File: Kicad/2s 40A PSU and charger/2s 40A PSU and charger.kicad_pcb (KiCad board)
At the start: 4 copper layers, 45 x 20 mm, 114 parts, among them J1 Keystone 3579, J10 G-Switch-GT-USB-7025, J11 1.27mm 4 pin socket, J12 USB, J2 JST XH-S Balance Plug, J3 Keystone 3579, J4 Keystone 3569, J5 Keystone 3569, J6 Keystone 3579, J7 Keystone 3579, J8 Keystone 3569, J9 Keystone 3569, Q1 PJA3430, Q2 PJA3430, Q3 Vishay sir404dp, or SiR500DP, Q4 PJA3430, Q5 PJA3430, Q6 Vishay sir404dp, or SiR500DP, U1 BQ76905RGRR, U2 AP63203WU, U3 BQ24780SRUYR, U5 THVD1420DRLR, U6 CH32X035G8U6, U7 TPS7A2633DRV

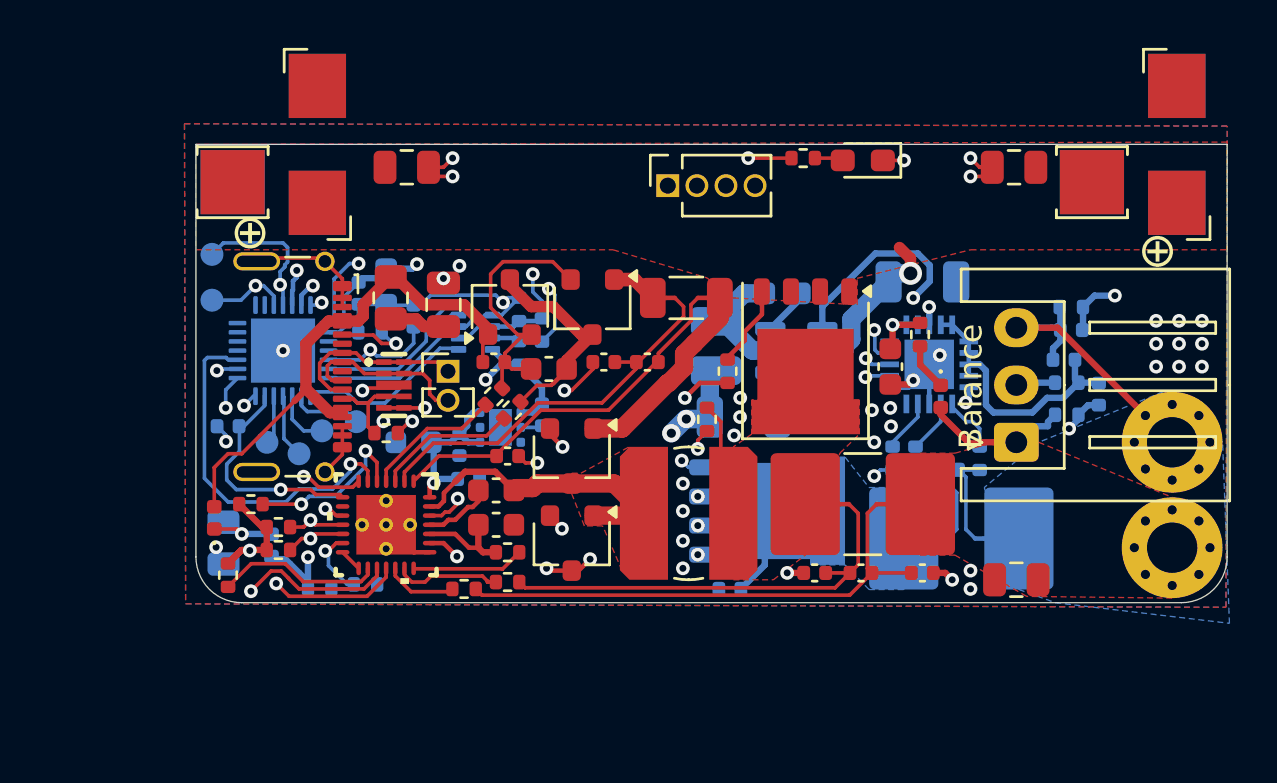
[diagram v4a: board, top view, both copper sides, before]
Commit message: Fixed incorrect mosfet pin assignments
This was an issue from the last test board I designed that I didn't catch. The mosfets have different pin assignments for drain, gate, and source, and I had messed those up in the schematic by choosing the wrong symbol. This should be fixed now
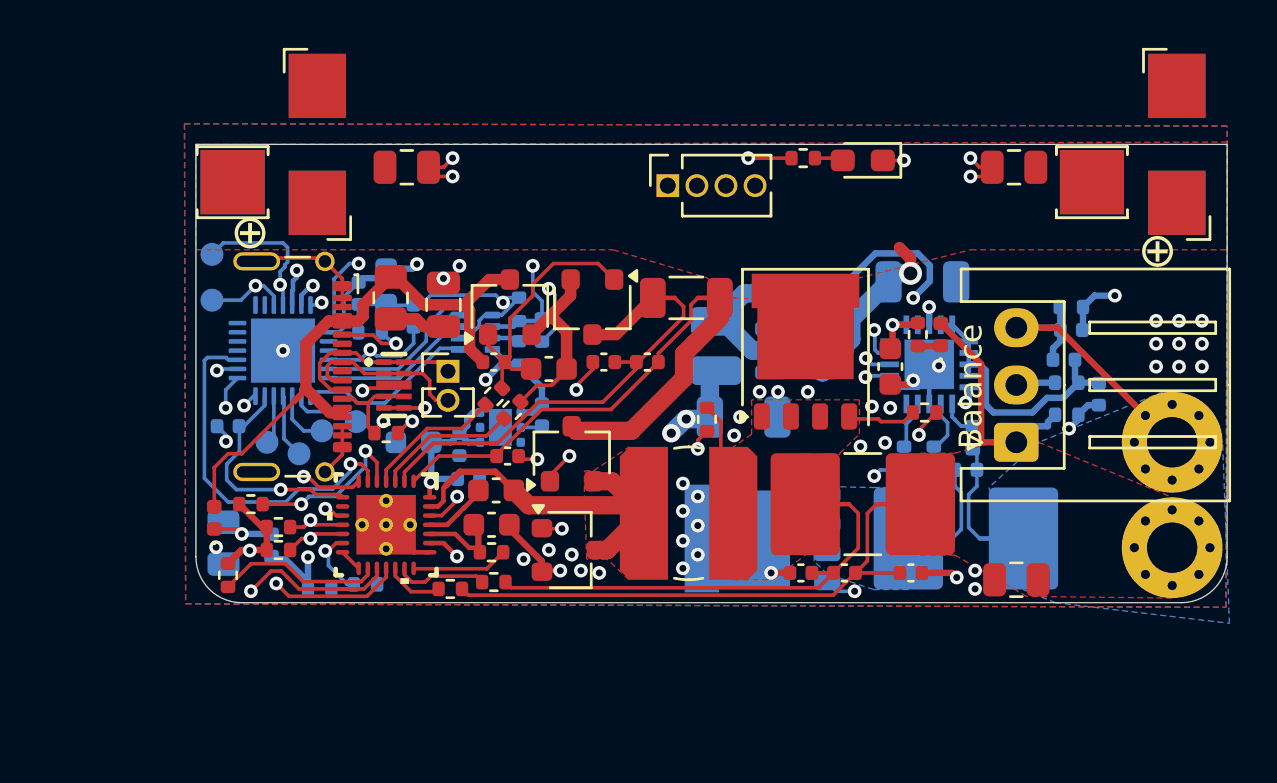
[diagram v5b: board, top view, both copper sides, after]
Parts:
- moved R10 8.79 mm to (139.9, 123.7), turned to 0 degrees
- moved C4 6.77 mm to (135.2, 125.8)
- moved D1 2.70 mm to (140.6, 120.3), turned to 90 degrees
- moved Q6 1.20 mm to (132.9, 129.2), turned to 180 degrees
- moved R4 0.95 mm to (142.0, 124.8)
- moved R5 0.80 mm to (140.3, 125.7)
- moved C3 0.80 mm to (141.7, 126.2)
- moved C22 0.72 mm to (136.4, 130.7)
- moved R20 0.70 mm to (121.0, 129.8)
- moved R21 0.60 mm to (121.1, 131.1)
- moved C21 0.60 mm to (134.5, 130.7)
- moved R22 0.60 mm to (119.2, 131.4)
- moved C23 0.50 mm to (139.3, 130.7)
- moved R6 0.50 mm to (139.0, 125.7)
- moved Q5 0.32 mm to (124.4, 129.7), turned to 0 degrees
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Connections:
- C4 pad 1: Net-(Q6-S) -> Net-(C4-Pad1)
- L2 pad 2: Net-(Q3-S) -> Net-(L2-Pad2)
- NT11 pad 1: Net-(Q6-S) -> Net-(C4-Pad1)
- NT6 pad 2: Net-(Q3-S) -> Net-(L2-Pad2)
- Q1 pad 1: /Battery Charger/IN -> Net-(Q1-G)
- Q1 pad 2: Net-(Q1-G) -> Net-(Q1-S)
- Q1 pad 3: Net-(Q1-S) -> /Battery Charger/IN
- Q2 pad 1: Net-(Q2-D) -> Net-(Q1-G)
- Q2 pad 2: Net-(Q1-G) -> Net-(Q1-S)
- Q2 pad 3: Net-(Q1-S) -> Net-(Q2-D)
- Q3 pad 1: /Battery Charger/MOTORPWR -> Net-(L2-Pad2)
- Q3 pad 2: /Battery Charger/MOTORPWR -> Net-(L2-Pad2)
- Q3 pad 3: /Battery Charger/MOTORPWR -> Net-(L2-Pad2)
- Q3 pad 5: Net-(Q3-S) -> /Battery Charger/MOTORPWR
- Q4 pad 1: Net-(Q4-D) -> Net-(Q4-G)
- Q4 pad 2: Net-(Q4-G) -> Net-(Q4-S)
- Q4 pad 3: Net-(Q4-S) -> Net-(Q4-D)
- Q5 pad 1: Net-(Q4-S) -> Net-(Q5-G)
- Q5 pad 2: Net-(Q5-G) -> GND
- Q5 pad 3: GND -> Net-(Q4-S)
- Q6 pad 1: GND -> Net-(C4-Pad1)
- Q6 pad 2: GND -> Net-(C4-Pad1)
- Q6 pad 3: GND -> Net-(C4-Pad1)
- Q6 pad 5: Net-(Q6-S) -> GND
- R12 pad 1: Net-(Q3-S) -> Net-(L2-Pad2)
- R14 pad 1: Net-(Q6-S) -> Net-(C4-Pad1)
- R18 pad 2: Net-(Q3-S) -> Net-(L2-Pad2)
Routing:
- net Net-(U3-BATDRV): track 29.5 -> 39.5 mm
- net GND: track 48.1 -> 53.6 mm, vias 43 -> 49
- net Net-(Q3-S): track 5.09 -> 0.00 mm
- net Net-(L2-Pad2): track 0.00 -> 5.09 mm
- net Net-(Q6-S): track 3.83 -> 0.00 mm
- net Net-(D1-A): track 2.62 -> 5.92 mm
- net Net-(Q4-S): track 14.8 -> 18.0 mm
- net Net-(Q6-G): track 10.6 -> 8.15 mm
- net /Battery Charger/IN: track 15.9 -> 18.2 mm
- net Net-(C4-Pad1): track 0.00 -> 1.51 mm
- net Net-(Q4-D): track 6.26 -> 7.61 mm
- net Net-(Q2-D): track 2.02 -> 3.30 mm
- net /Battery Balancer/-BAT: track 33.3 -> 32.1 mm
- net Net-(D1-K): track 2.08 -> 1.01 mm
- net Net-(Q1-S): track 6.71 -> 5.72 mm
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- added copper zone on B.Cu, net Net-(C4-Pad1)
- added copper zone on F.Cu, net Net-(L2-Pad2)
- removed copper zone on F.Cu, net Net-(Q3-S)
- removed copper zone on B.Cu, net Net-(Q6-S)

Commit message: Final tweaks, capacitor placement and GND keepouts
I tried my best to isolate signal grounds from the power paths. I also added a bunch of ground keepouts to help isolate.
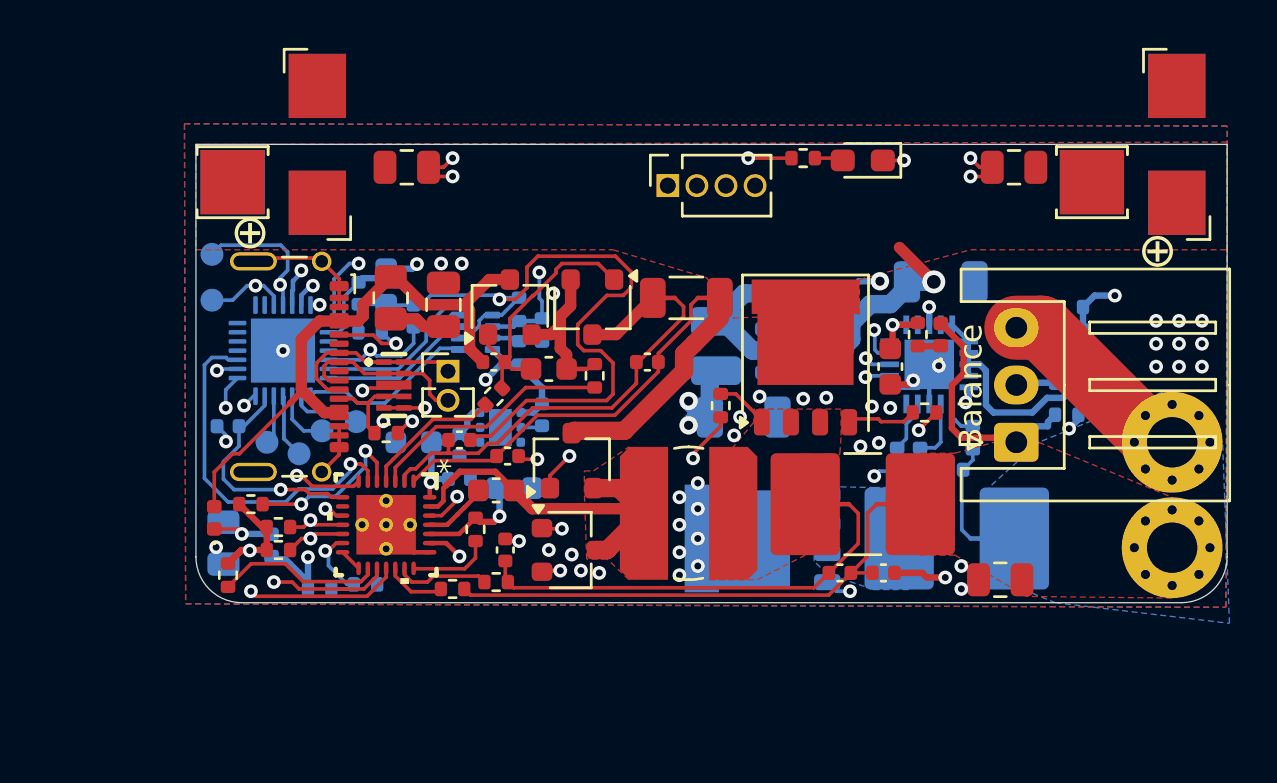
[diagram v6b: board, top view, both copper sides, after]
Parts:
- C24: moved to B.Cu
- moved C21 12.9 mm to (121.6, 129.7), turned to -90 degrees
- moved C9 7.16 mm to (119.6, 124.9), turned to 180 degrees
- moved R7 3.90 mm to (125.5, 122.1), turned to 90 degrees
- moved C24 1.89 mm to (122.0, 127.0)
- moved R20 1.22 mm to (120.3, 128.8), turned to 90 degrees
- moved NT14 1.21 mm to (124.9, 121.8), turned to 180 degrees
- moved C23 1.20 mm to (138.1, 130.7)
- moved R12 0.85 mm to (131.0, 123.4)
- moved C28 0.80 mm to (140.6, 118.0)
- moved C20 0.70 mm to (143.2, 131.0)
- moved R5 0.60 mm to (139.7, 125.8)
- moved C3 0.60 mm to (141.1, 126.2)
- moved C15 0.40 mm to (119.6, 126.6)
- moved NT1 0.40 mm to (142.1, 129.2)
- moved NT11 0.40 mm to (140.5, 129.2)
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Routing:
- net /Connectors/3.3v: track 63.6 -> 33.5 mm
- net GND: track 53.6 -> 72.1 mm, vias 49 -> 48
- net Net-(U3-CMSRC): track 6.14 -> 10.8 mm
- net /Battery Balancer/Balancer Alert: track 35.3 -> 37.8 mm
- net Net-(L2-Pad2): track 5.09 -> 3.13 mm
- net Net-(U3-BATSRC): track 30.2 -> 28.5 mm
- net /Battery Charger/MOTORPWR: track 8.54 -> 10.2 mm
- net Net-(NT14-Pad1): track 1.75 -> 0.50 mm
- net Net-(C22-Pad2): track 23.0 -> 21.8 mm
- net /Battery Charger/REGN: track 3.68 -> 4.80 mm, vias 0 -> 1
- net /Connectors/RS485-: track 19.3 -> 18.5 mm
- net Net-(U3-BATDRV): track 39.5 -> 40.3 mm
- net Net-(D1-A): track 5.92 -> 6.65 mm
- net /Battery Charger/Charger IADP: track 14.5 -> 15.2 mm
- net /Battery Balancer/+BAT: track 40.3 -> 39.7 mm
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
